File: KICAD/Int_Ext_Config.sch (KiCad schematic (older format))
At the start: 9 parts

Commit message: review w/ jmt
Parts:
- gave numbers to parts that had none: 9
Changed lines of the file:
@@
 $Descr A4 11693 8268
 encoding utf-8
-Sheet 15 17
+Sheet 14 17
 Title ""
 Date ""
@@
 $EndDescr
 $Comp
-L power:GND #PWR0109
+L power:GND #PWR094
 U 1 1 61886094
 P 7700 3750
-F 0 "#PWR0109" H 7700 3500 50  0001 C CNN
+F 0 "#PWR094" H 7700 3500 50  0001 C CNN
 F 1 "GND" H 7705 3577 50  0000 C CNN
 F 2 "" H 7700 3750 50  0001 C CNN
@@
 	3750 4250 4050 4250
 $Comp
-L Connector_Generic:Conn_02x16_Odd_Even J?
+L Connector_Generic:Conn_02x16_Odd_Even J9
 U 1 1 61332892
 P 3450 4650
-F 0 "J?" H 3500 5567 50  0000 C CNN
+F 0 "J9" H 3500 5567 50  0000 C CNN
 F 1 "Conn_02x16_Odd_Even" H 3500 5476 50  0000 C CNN
 F 2 "" H 3450 4650 50  0001 C CNN
@@
 $EndComp
 $Comp
-L power:VCC #PWR?
+L power:VCC #PWR092
 U 1 1 6133D413
 P 4050 3800
-F 0 "#PWR?" H 4050 3650 50  0001 C CNN
+F 0 "#PWR092" H 4050 3650 50  0001 C CNN
 F 1 "VCC" H 4065 3973 50  0000 C CNN
 F 2 "" H 4050 3800 50  0001 C CNN
@@
 Connection ~ 4050 3950
 $Comp
-L Sesame:VREF #PWR?
+L Sesame:VREF #PWR093
 U 1 1 6134066E
 P 4300 3800
-F 0 "#PWR?" H 4300 3650 50  0001 C CNN
+F 0 "#PWR093" H 4300 3650 50  0001 C CNN
 F 1 "VREF" H 4315 3973 50  0000 C CNN
 F 2 "" H 4300 3800 50  0001 C CNN
@@
 CC_CV_Mode
 $Comp
-L power:GND #PWR?
+L power:GND #PWR091
 U 1 1 6134A761
 P 3150 5550
-F 0 "#PWR?" H 3150 5300 50  0001 C CNN
+F 0 "#PWR091" H 3150 5300 50  0001 C CNN
 F 1 "GND" H 3155 5377 50  0000 C CNN
 F 2 "" H 3150 5550 50  0001 C CNN
@@
 	3150 5350 3150 5250
 $Comp
-L Device:Jumper_NC_Dual JP?
+L Device:Jumper_NC_Dual JP12
 U 1 1 61366A29
 P 8150 3650
-F 0 "JP?" H 8150 3889 50  0000 C CNN
+F 0 "JP12" H 8150 3889 50  0000 C CNN
 F 1 "Jumper_NC_Dual" H 8150 3798 50  0000 C CNN
 F 2 "" H 8150 3650 50  0001 C CNN
@@
 $EndComp
 $Comp
-L power:VCC #PWR?
+L power:VCC #PWR095
 U 1 1 6136D0ED
 P 8600 3600
-F 0 "#PWR?" H 8600 3450 50  0001 C CNN
+F 0 "#PWR095" H 8600 3450 50  0001 C CNN
 F 1 "VCC" H 8615 3773 50  0000 C CNN
 F 2 "" H 8600 3600 50  0001 C CNN
@@
 ~Ext_PWM
 $Comp
-L Device:R R?
+L Device:R R76
 U 1 1 6137F2F0
 P 8150 4000
-F 0 "R?" H 8220 4046 50  0000 L CNN
+F 0 "R76" H 8220 4046 50  0000 L CNN
 F 1 "10k" H 8220 3955 50  0000 L CNN
 F 2 "" V 8080 4000 50  0001 C CNN
@@
 	8150 4250 8150 4150
 $Comp
-L power:GND #PWR?
+L power:GND #PWR096
 U 1 1 61386A80
 P 8850 3750
-F 0 "#PWR?" H 8850 3500 50  0001 C CNN
+F 0 "#PWR096" H 8850 3500 50  0001 C CNN
 F 1 "GND" H 8855 3577 50  0000 C CNN
 F 2 "" H 8850 3750 50  0001 C CNN
@@
 $EndComp
 $Comp
-L Device:Jumper_NC_Dual JP?
+L Device:Jumper_NC_Dual JP13
 U 1 1 61386A86
 P 9300 3650
-F 0 "JP?" H 9300 3889 50  0000 C CNN
+F 0 "JP13" H 9300 3889 50  0000 C CNN
 F 1 "Jumper_NC_Dual" H 9300 3798 50  0000 C CNN
 F 2 "" H 9300 3650 50  0001 C CNN
@@
 $EndComp
 $Comp
-L power:VCC #PWR?
+L power:VCC #PWR097
 U 1 1 61386A8C
 P 9750 3600
-F 0 "#PWR?" H 9750 3450 50  0001 C CNN
+F 0 "#PWR097" H 9750 3450 50  0001 C CNN
 F 1 "VCC" H 9765 3773 50  0000 C CNN
 F 2 "" H 9750 3600 50  0001 C CNN
@@
 	8850 3650 9050 3650
 $Comp
-L Device:R R?
+L Device:R R77
 U 1 1 61386A97
 P 9300 4000
-F 0 "R?" H 9370 4046 50  0000 L CNN
+F 0 "R77" H 9370 4046 50  0000 L CNN
 F 1 "10k" H 9370 3955 50  0000 L CNN
 F 2 "" V 9230 4000 50  0001 C CNN
@@
 	9300 4250 9300 4150
 $Comp
-L power:GND #PWR?
+L power:GND #PWR098
 U 1 1 6138E72F
 P 10000 3750
-F 0 "#PWR?" H 10000 3500 50  0001 C CNN
+F 0 "#PWR098" H 10000 3500 50  0001 C CNN
 F 1 "GND" H 10005 3577 50  0000 C CNN
 F 2 "" H 10000 3750 50  0001 C CNN
@@
 $EndComp
 $Comp
-L Device:Jumper_NC_Dual JP?
+L Device:Jumper_NC_Dual JP14
 U 1 1 6138E735
 P 10450 3650
-F 0 "JP?" H 10450 3889 50  0000 C CNN
+F 0 "JP14" H 10450 3889 50  0000 C CNN
 F 1 "Jumper_NC_Dual" H 10450 3798 50  0000 C CNN
 F 2 "" H 10450 3650 50  0001 C CNN
@@
 $EndComp
 $Comp
-L power:VCC #PWR?
+L power:VCC #PWR099
 U 1 1 6138E73B
 P 10900 3600
-F 0 "#PWR?" H 10900 3450 50  0001 C CNN
+F 0 "#PWR099" H 10900 3450 50  0001 C CNN
 F 1 "VCC" H 10915 3773 50  0000 C CNN
 F 2 "" H 10900 3600 50  0001 C CNN
@@
 	10000 3650 10200 3650
 $Comp
-L Device:R R?
+L Device:R R78
 U 1 1 6138E745
 P 10450 4000
-F 0 "R?" H 10520 4046 50  0000 L CNN
+F 0 "R78" H 10520 4046 50  0000 L CNN
 F 1 "10k" H 10520 3955 50  0000 L CNN
 F 2 "" V 10380 4000 50  0001 C CNN
@@
 Connection ~ 10450 4250
 $Comp
-L Device:Jumper_NC_Dual JP?
+L Device:Jumper_NC_Dual JP11
 U 1 1 6139D414
 P 6850 3650
-F 0 "JP?" H 6850 3889 50  0000 C CNN
+F 0 "JP11" H 6850 3889 50  0000 C CNN
 F 1 "Jumper_NC_Dual" H 6850 3798 50  0000 C CNN
 F 2 "" H 6850 3650 50  0001 C CNN
@@
 ~INT_PWM
 $Comp
-L Device:Jumper_NC_Dual JP?
+L Device:Jumper_NC_Dual JP10
 U 1 1 613A5DB8
 P 5450 3650
-F 0 "JP?" H 5450 3889 50  0000 C CNN
+F 0 "JP10" H 5450 3889 50  0000 C CNN
 F 1 "Jumper_NC_Dual" H 5450 3798 50  0000 C CNN
 F 2 "" H 5450 3650 50  0001 C CNN

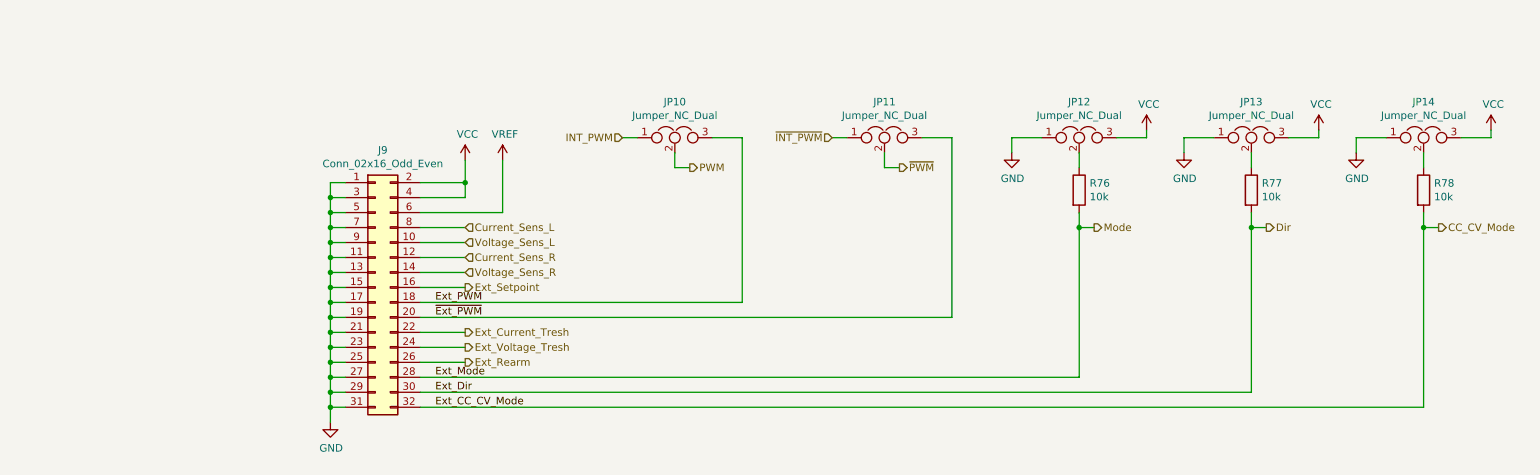
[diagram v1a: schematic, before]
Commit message: edit footprints by jmt
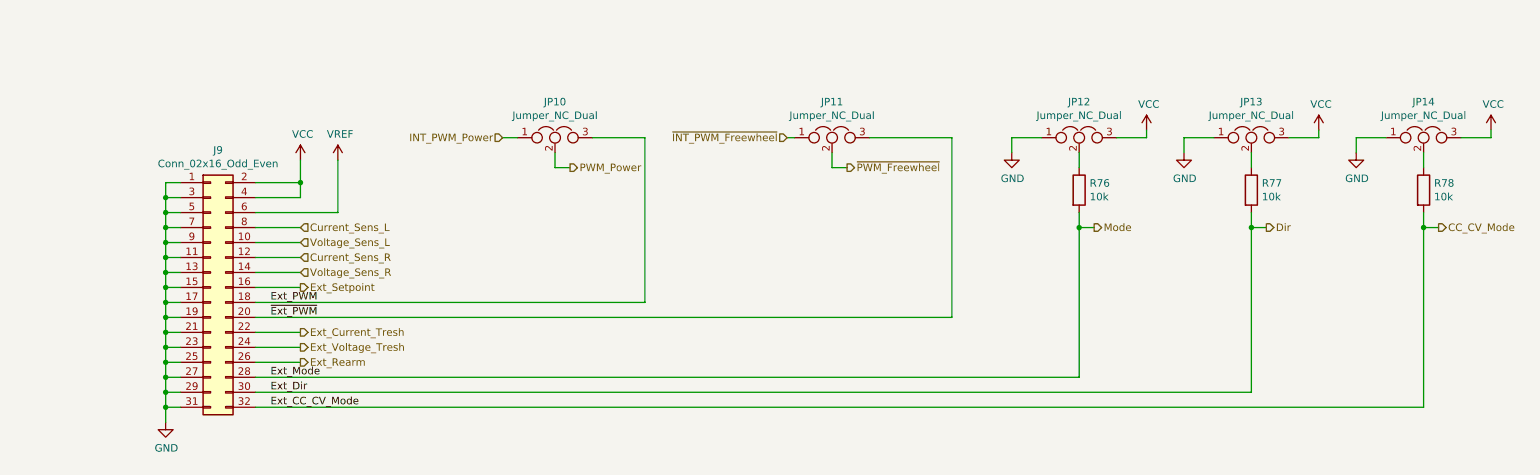
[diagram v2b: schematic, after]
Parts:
- J9: footprint (none) -> Connector_PinHeader_2.54mm:PinHeader_2x16_P2.54mm_Vertical
- JP10, JP11, JP12, JP13, JP14: footprint (none) -> Connector_PinHeader_2.54mm:PinHeader_1x03_P2.54mm_Vertical
- R76, R77, R78: footprint (none) -> Resistor_SMD:R_0805_2012Metric_Pad1.15x1.40mm_HandSolder
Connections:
- net INT_PWM renamed INT_PWM_Power
- net PWM renamed PWM_Power
- net ~INT_PWM renamed ~INT_PWM_Freewheel
- net ~PWM renamed ~PWM_Freewheel
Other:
- moved on the sheet: J9, JP10, JP11

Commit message: route + work on djd
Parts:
- J9: footprint Connector_PinHeader_2.54mm:PinHeader_2x16_P2.54mm_Vertical -> Connector_PinSocket_2.54mm:PinSocket_2x16_P2.54mm_Vertical
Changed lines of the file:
@@
 F 0 "J9" H 2400 5567 50  0000 C CNN
 F 1 "Conn_02x16_Odd_Even" H 2400 5476 50  0000 C CNN
-F 2 "Connector_PinHeader_2.54mm:PinHeader_2x16_P2.54mm_Vertical" H 2350 4650 50  0001 C CNN
+F 2 "Connector_PinSocket_2.54mm:PinSocket_2x16_P2.54mm_Vertical" H 2350 4650 50  0001 C CNN
 F 3 "~" H 2350 4650 50  0001 C CNN
 	1    2350 4650

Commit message: added footprint for sepic coil + no more errors in netlist
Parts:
- R76, R77, R78: footprint Resistor_SMD:R_0805_2012Metric_Pad1.15x1.40mm_HandSolder -> Sesame_footprint:R_0805_2012Metric_Pad1.20x1.40mm_HandSolder
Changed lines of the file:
@@
 F 0 "R76" H 8220 4046 50  0000 L CNN
 F 1 "10k" H 8220 3955 50  0000 L CNN
-F 2 "Resistor_SMD:R_0805_2012Metric_Pad1.15x1.40mm_HandSolder" V 8080 4000 50  0001 C CNN
+F 2 "Sesame_footprint:R_0805_2012Metric_Pad1.20x1.40mm_HandSolder" V 8080 4000 50  0001 C CNN
 F 3 "~" H 8150 4000 50  0001 C CNN
 	1    8150 4000
@@
 F 0 "R77" H 9370 4046 50  0000 L CNN
 F 1 "10k" H 9370 3955 50  0000 L CNN
-F 2 "Resistor_SMD:R_0805_2012Metric_Pad1.15x1.40mm_HandSolder" V 9230 4000 50  0001 C CNN
+F 2 "Sesame_footprint:R_0805_2012Metric_Pad1.20x1.40mm_HandSolder" V 9230 4000 50  0001 C CNN
 F 3 "~" H 9300 4000 50  0001 C CNN
 	1    9300 4000
@@
 F 0 "R78" H 10520 4046 50  0000 L CNN
 F 1 "10k" H 10520 3955 50  0000 L CNN
-F 2 "Resistor_SMD:R_0805_2012Metric_Pad1.15x1.40mm_HandSolder" V 10380 4000 50  0001 C CNN
+F 2 "Sesame_footprint:R_0805_2012Metric_Pad1.20x1.40mm_HandSolder" V 10380 4000 50  0001 C CNN
 F 3 "~" H 10450 4000 50  0001 C CNN
 	1    10450 4000

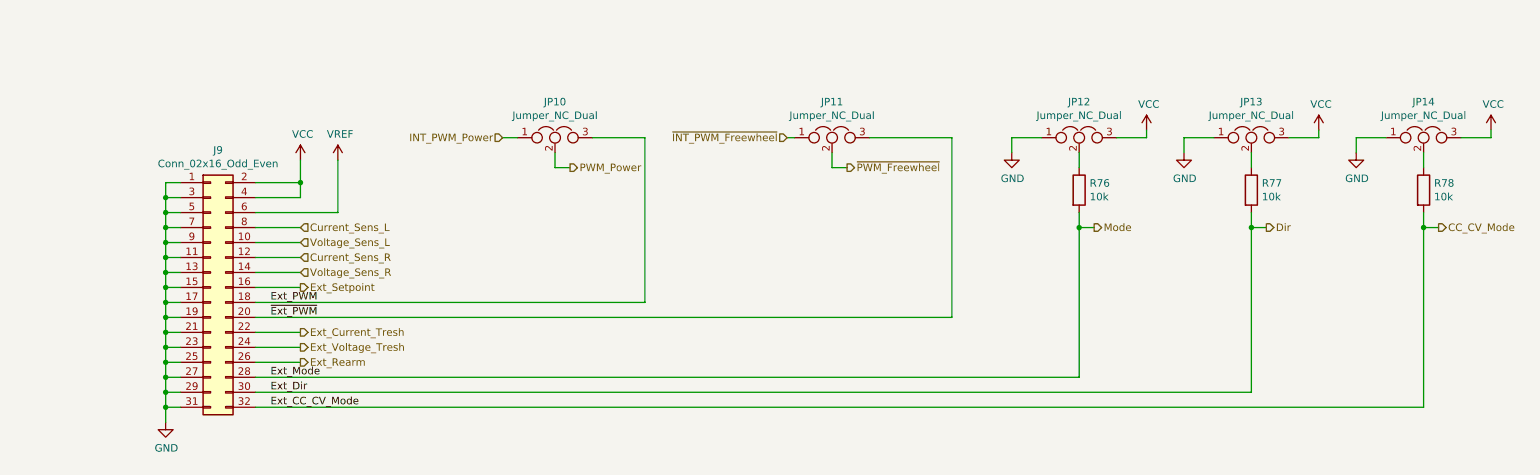
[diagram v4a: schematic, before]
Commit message: 95 conn. doing analog switchs
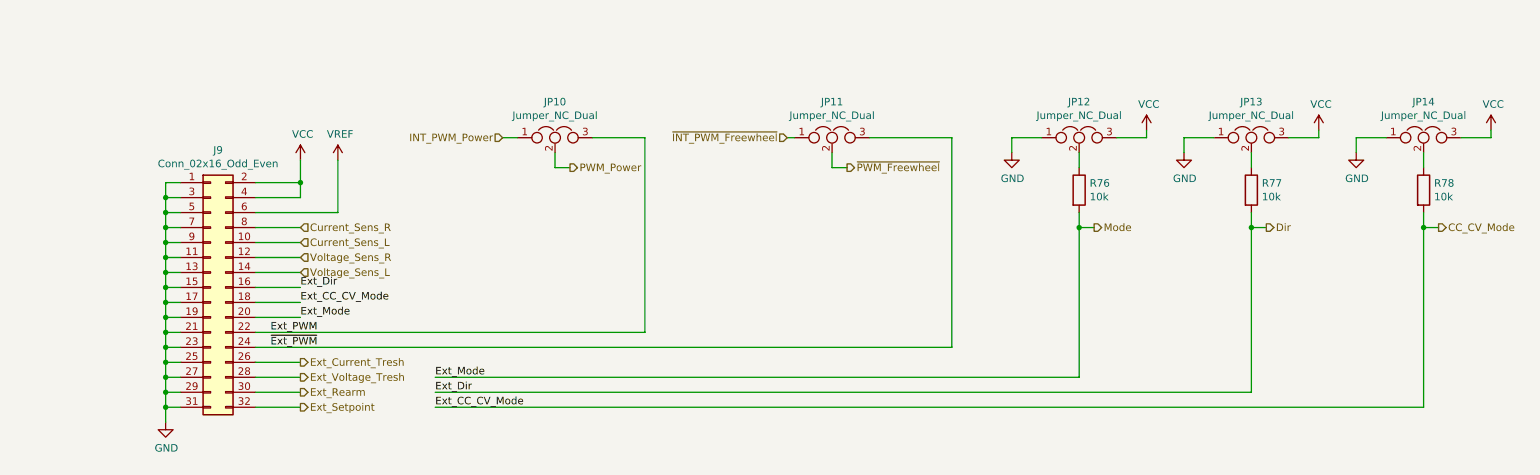
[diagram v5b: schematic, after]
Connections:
- net CC_CV_Mode: now also J9.18 (Pin_18); no longer J9.32 (Pin_32)
- net Current_Sens_L: now also J9.10 (Pin_10); no longer J9.8 (Pin_8)
- net Current_Sens_R: now also J9.8 (Pin_8); no longer J9.12 (Pin_12)
- net Dir: now also J9.16 (Pin_16); no longer J9.30 (Pin_30)
- net Ext_Current_Tresh: now also J9.26 (Pin_26); no longer J9.22 (Pin_22)
- net Ext_PWM: now also J9.22 (Pin_22); no longer J9.18 (Pin_18)
- net Ext_Rearm: now also J9.30 (Pin_30); no longer J9.26 (Pin_26)
- net Ext_Setpoint: now also J9.32 (Pin_32); no longer J9.16 (Pin_16)
- net Ext_Voltage_Tresh: now also J9.28 (Pin_28); no longer J9.24 (Pin_24)
- net Mode: now also J9.20 (Pin_20); no longer J9.28 (Pin_28)
- net Voltage_Sens_L: now also J9.14 (Pin_14); no longer J9.10 (Pin_10)
- net Voltage_Sens_R: now also J9.12 (Pin_12); no longer J9.14 (Pin_14)
- net ~Ext_PWM: now also J9.24 (Pin_24); no longer J9.20 (Pin_20)

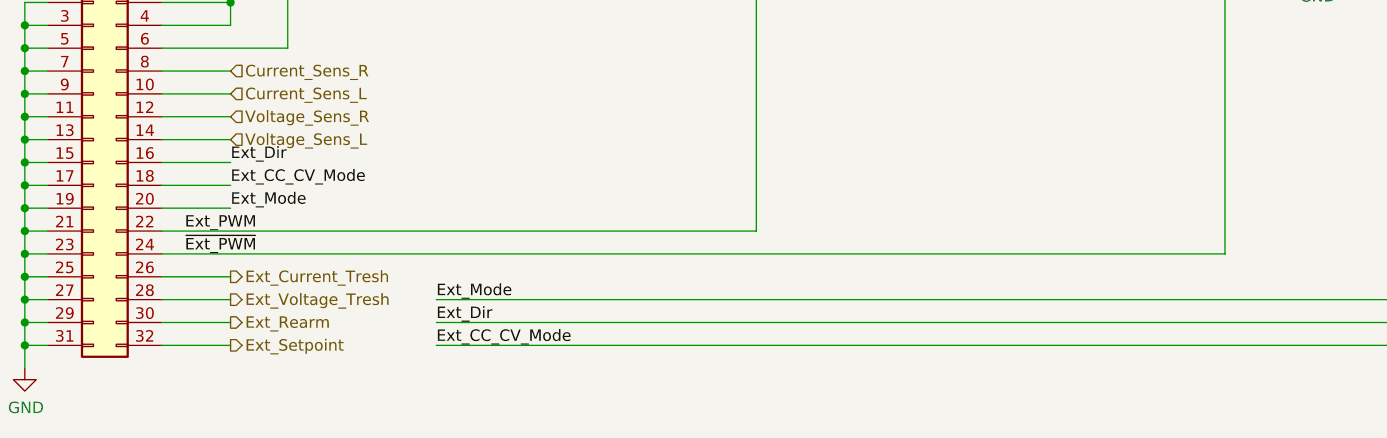
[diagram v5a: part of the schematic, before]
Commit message: 30 conn. changed again the pinout of io connector
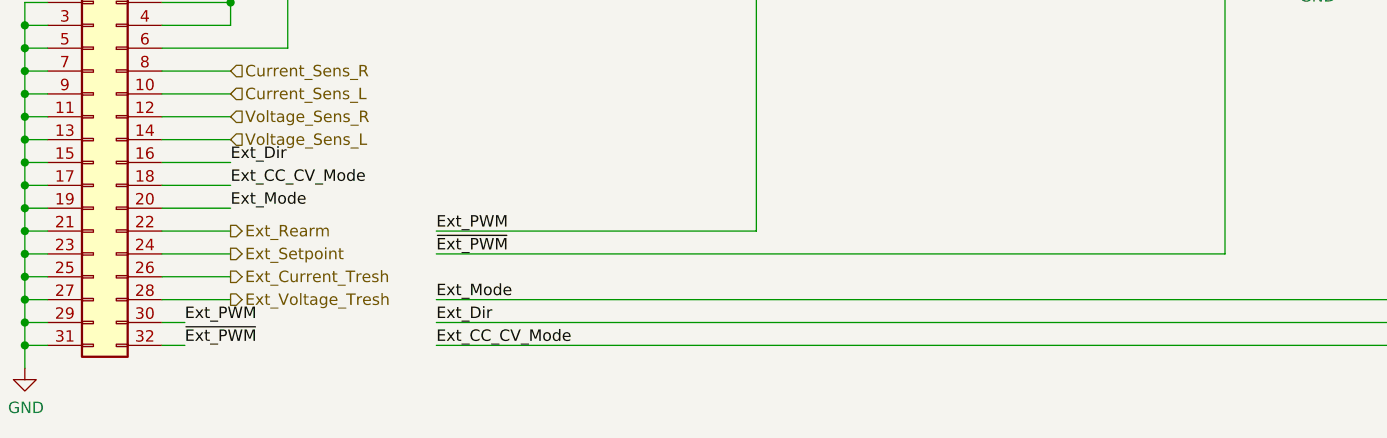
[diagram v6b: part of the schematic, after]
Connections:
- net Ext_PWM: now also J9.30 (Pin_30); no longer J9.22 (Pin_22)
- net Ext_Rearm: now also J9.22 (Pin_22); no longer J9.30 (Pin_30)
- net Ext_Setpoint: now also J9.24 (Pin_24); no longer J9.32 (Pin_32)
- net ~Ext_PWM: now also J9.32 (Pin_32); no longer J9.24 (Pin_24)
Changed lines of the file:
@@
 Wire Wire Line
 	3200 3800 3200 4150
-Text HLabel 2950 5450 2    50   Output ~ 0
+Text HLabel 2950 5050 2    50   Output ~ 0
 Ext_Setpoint
 Text HLabel 2950 5150 2    50   Output ~ 0
@@
 Text HLabel 8250 4250 2    50   Output ~ 0
 Mode
-Text HLabel 2950 5350 2    50   Output ~ 0
+Text HLabel 2950 4950 2    50   Output ~ 0
 Ext_Rearm
-Text Label 2750 4950 0    50   ~ 0
-Ext_PWM
-Text Label 2750 5050 0    50   ~ 0
-~Ext_PWM
 $Comp
 L Device:R R76
@@
 ~PWM_Freewheel
 Wire Wire Line
+	2950 4950 2650 4950
+Wire Wire Line
+	10450 5450 10450 4250
+Wire Wire Line
+	9300 5350 9300 4250
+Wire Wire Line
+	8150 5250 8150 4250
+Wire Wire Line
+	3850 5450 10450 5450
+Wire Wire Line
+	3850 5350 9300 5350
+Wire Wire Line
+	3850 5250 8150 5250
+Text Label 3850 5450 0    50   ~ 0
+Ext_CC_CV_Mode
+Text Label 3850 5350 0    50   ~ 0
+Ext_Dir
+Text Label 3850 5250 0    50   ~ 0
+Ext_Mode
+Wire Wire Line
+	2950 5050 2650 5050
+Text Label 2950 4850 0    50   ~ 0
+Ext_Mode
+Text Label 2950 4650 0    50   ~ 0
+Ext_Dir
+Text Label 2950 4750 0    50   ~ 0
+Ext_CC_CV_Mode
+Text Label 2750 5450 0    50   ~ 0
+~Ext_PWM
+Text Label 2750 5350 0    50   ~ 0
+Ext_PWM
+Wire Wire Line
 	2050 4350 2150 4350
 Wire Wire Line
@@
 	2150 5350 2050 5350
 Wire Wire Line
+	2950 5250 2650 5250
+Wire Wire Line
 	2150 5250 2050 5250
 Wire Wire Line
-	2950 5350 2650 5350
+	2950 5150 2650 5150
 Wire Wire Line
 	2150 5150 2050 5150
 Wire Wire Line
-	2950 5250 2650 5250
-Wire Wire Line
 	2150 5050 2050 5050
 Wire Wire Line
-	2950 5150 2650 5150
-Wire Wire Line
 	2150 4950 2050 4950
 Wire Wire Line
-	2650 5050 7300 5050
+	2650 4850 2950 4850
 Wire Wire Line
 	2650 3950 2950 3950
@@
 	2150 4850 2050 4850
 Wire Wire Line
-	2650 4950 5250 4950
+	2950 4750 2650 4750
 Wire Wire Line
 	2150 4750 2050 4750
@@
 	2050 3950 2150 3950
 Wire Wire Line
-	10450 5450 10450 4250
-Wire Wire Line
-	9300 5350 9300 4250
-Wire Wire Line
-	8150 5250 8150 4250
+	5250 3650 5250 4950
+Wire Wire Line
+	7300 3650 7300 5050
 $Comp
 L Connector_Generic:Conn_02x16_Odd_Even J9
@@
 $EndComp
 Wire Wire Line
-	3850 5450 10450 5450
-Wire Wire Line
-	3850 5350 9300 5350
-Wire Wire Line
-	3850 5250 8150 5250
-Text Label 3850 5450 0    50   ~ 0
-Ext_CC_CV_Mode
-Text Label 3850 5350 0    50   ~ 0
-Ext_Dir
-Text Label 3850 5250 0    50   ~ 0
-Ext_Mode
-Wire Wire Line
-	2950 5450 2650 5450
-Wire Wire Line
-	5250 3650 5250 4950
-Wire Wire Line
-	7300 3650 7300 5050
-Text Label 2950 4850 0    50   ~ 0
-Ext_Mode
-Text Label 2950 4650 0    50   ~ 0
-Ext_Dir
-Text Label 2950 4750 0    50   ~ 0
-Ext_CC_CV_Mode
-Wire Wire Line
-	2950 4750 2650 4750
-Wire Wire Line
-	2650 4850 2950 4850
+	3850 4950 5250 4950
+Wire Wire Line
+	3850 5050 7300 5050
+Text Label 3850 5050 0    50   ~ 0
+~Ext_PWM
+Text Label 3850 4950 0    50   ~ 0
+Ext_PWM
+Wire Wire Line
+	2750 5350 2650 5350
+Wire Wire Line
+	2650 5450 2750 5450
 $EndSCHEMATC

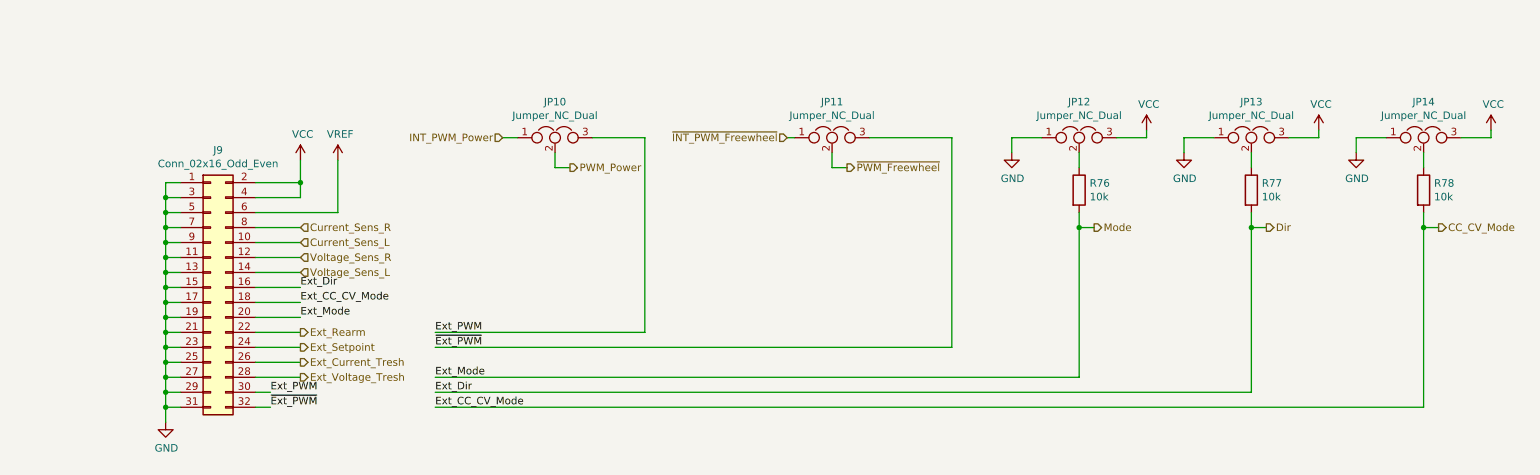
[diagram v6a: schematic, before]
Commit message: correction on the ext config
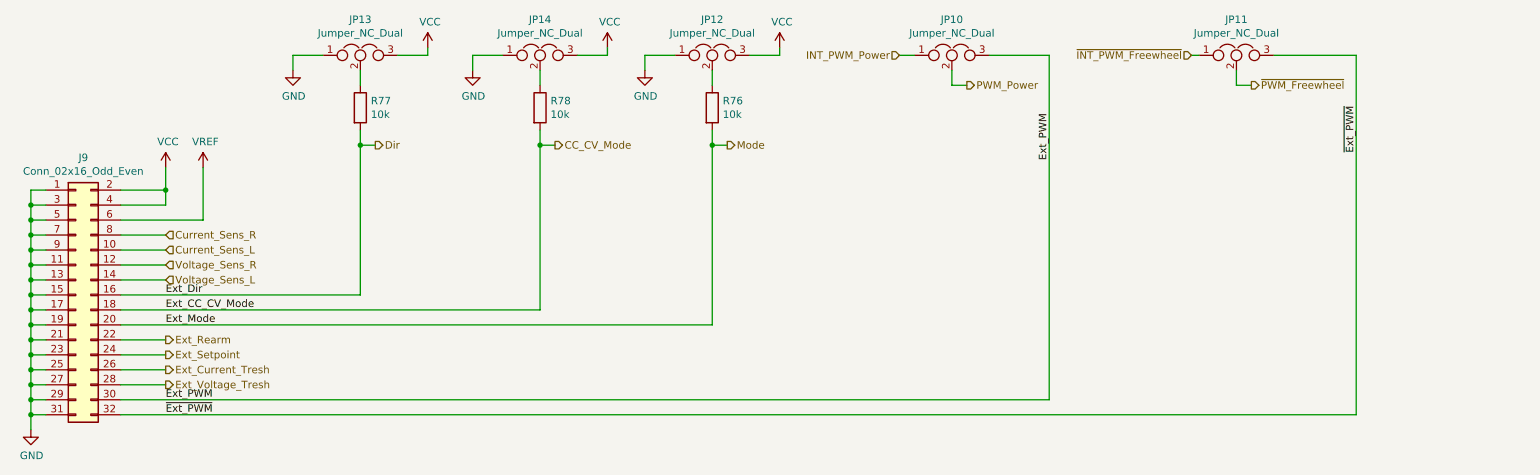
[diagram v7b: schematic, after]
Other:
- moved on the sheet: J9, JP10, JP11, JP12, JP13, JP14, R76, R77, R78
